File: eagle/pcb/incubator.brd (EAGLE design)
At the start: 99.1 x 63.5 mm, 56 parts, among them IC1 MCP1703-50, J2 RJ12RIGHTANGLE-I2C, J7 22--02, Q1 BSP75, Q5 BSP75, X2 8MHz, X4 MINI-USB

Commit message: routing in progress
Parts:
- added D2: 1N581D1206, lpatiny:LED-1206
- moved D4 15.1 mm to (75.6, 44.5), turned to 90 degrees
- moved D7 13.5 mm to (71.8, 44.5), turned to 90 degrees
- moved D1 13.1 mm to (81.9, 45.7), turned to 0 degrees
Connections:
- removed net N$3: CU7.1, D1.C, D4.C, D7.C, D8.C, IC1.1
- new net I2C+5V: D2.A, J2.+5V
- new net N$123: CU7.1, D1.C, D2.C, D4.C, D7.C, D8.C, IC1.1
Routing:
- net VUSB: track 104.6 -> 69.3 mm
- net D12*: track 0.00 -> 22.3 mm
- net N$3: track 0.55 -> 0.00 mm
- net N$123: track 0.00 -> 0.55 mm

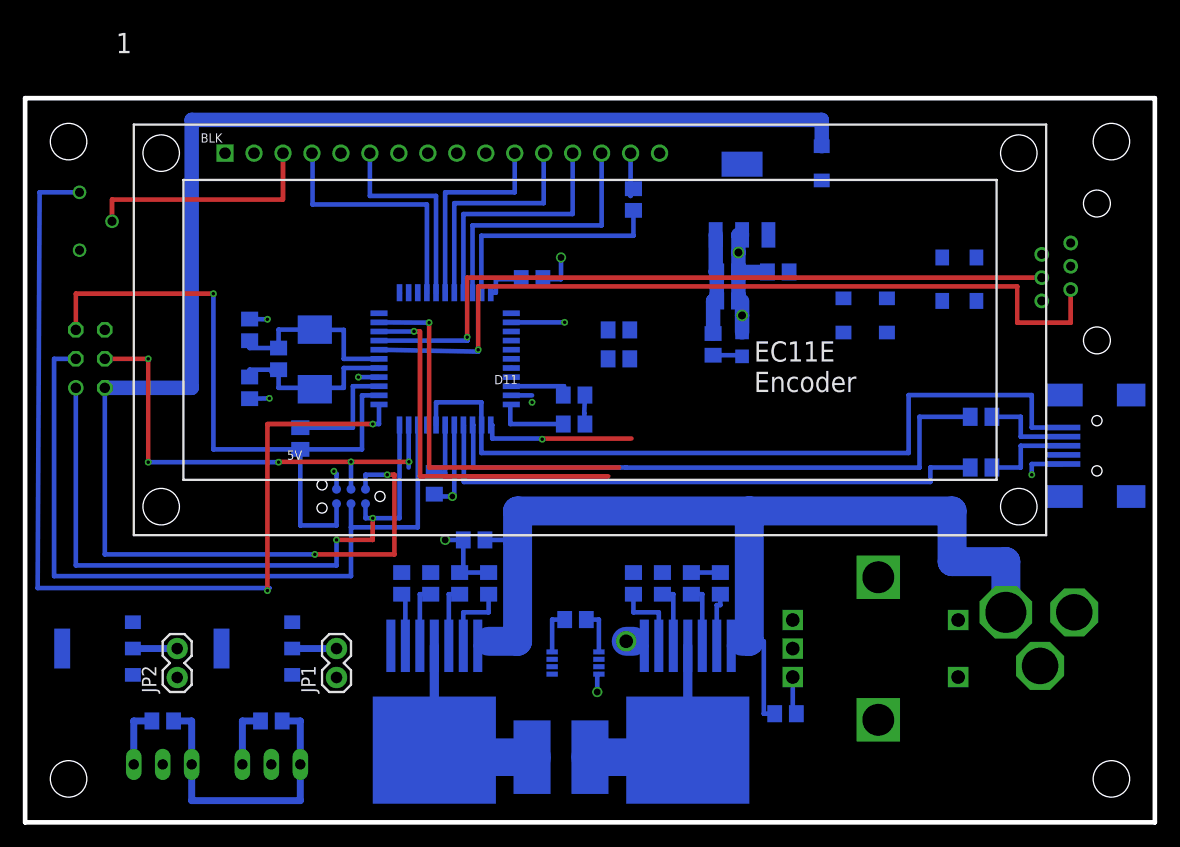
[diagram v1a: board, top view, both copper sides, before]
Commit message: first version of the incubator
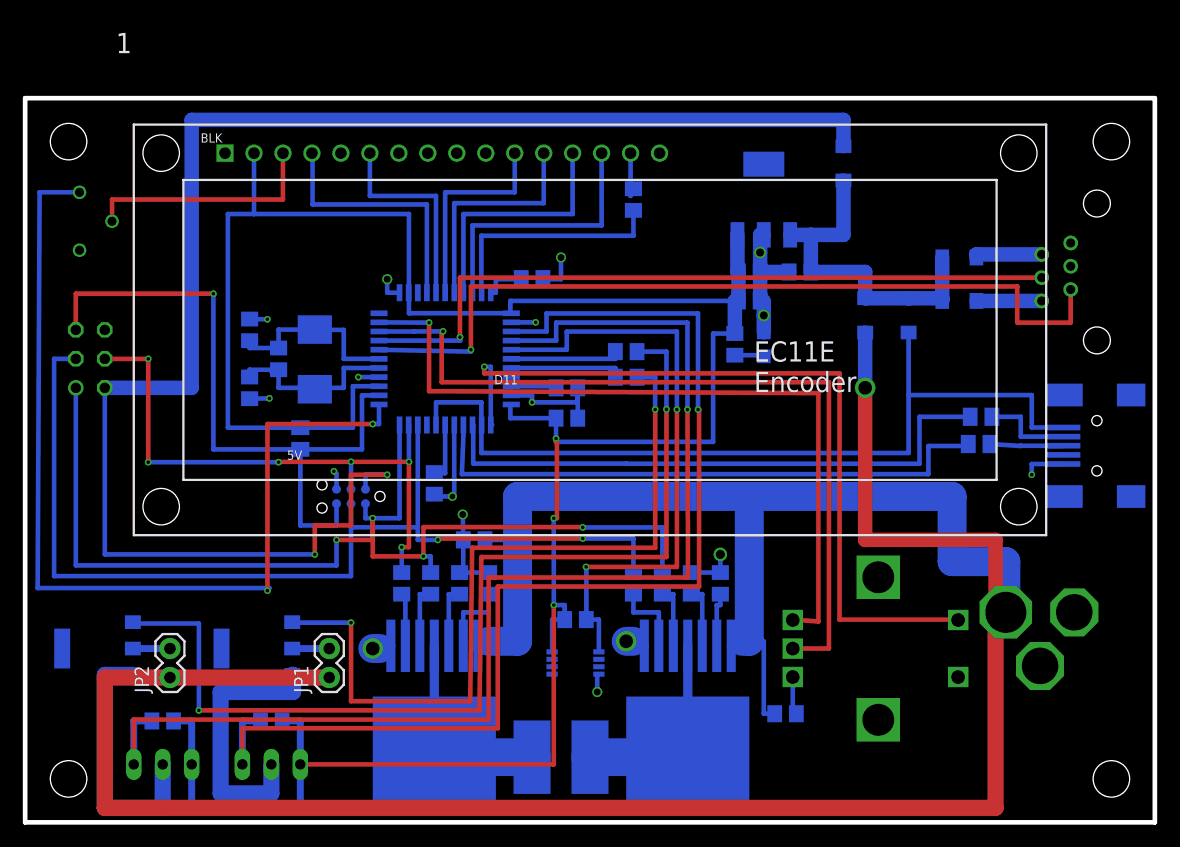
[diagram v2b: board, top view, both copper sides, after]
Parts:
- moved R1 4.20 mm to (52.7, 39.0), turned to 180 degrees
- moved RUSB2 2.06 mm to (83.6, 33.2)
- moved CU1 1.91 mm to (63.5, 45.7)
- moved CU8 1.91 mm to (63.5, 48.3)
- moved D4 1.91 mm to (77.5, 44.5)
- moved D7 1.91 mm to (73.7, 44.5)
- moved D8 1.91 mm to (71.8, 57.8)
- moved IC1 1.90 mm to (64.8, 54.6)
- moved LDPW5 1.90 mm to (64.8, 41.9)
- moved R13 1.90 mm to (62.2, 41.9)
- moved CU7 1.90 mm to (67.9, 48.3)
- moved C10 0.90 mm to (47.5, 38.1)
- moved R2 0.90 mm to (52.7, 41.3)
- moved C12 0.82 mm to (47.5, 35.4)
- moved JP2 0.64 mm to (12.7, 12.7)
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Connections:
- net A0: now also JP5.3, RT3.2; no longer R1.1
- net A1: now also JP4.3, RT1.2; no longer R2.1
- net A3: now also R2.1; no longer JP4.3, RT1.2
- net A4: now also R1.1; no longer JP5.3, RT3.2
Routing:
- net +12V: track 91.9 -> 258.9 mm, vias 0 -> 1
- net VCC: track 56.9 -> 223.5 mm, vias 0 -> 3
- net A1: track 0.00 -> 109.8 mm, vias 0 -> 1
- net A0: track 0.00 -> 103.0 mm, vias 0 -> 1
- net N$20: track 0.00 -> 88.4 mm, vias 0 -> 2
- net N$9: track 0.00 -> 68.6 mm, vias 0 -> 2
- net GND: track 60.3 -> 116.7 mm, vias 14 -> 17
- net D7*: track 13.7 -> 69.6 mm
- net A2: track 3.94 -> 53.3 mm, vias 0 -> 2
- net RX: track 32.8 -> 70.7 mm
- net MISO: track 58.2 -> 95.5 mm, vias 2 -> 4
- net TX: track 33.7 -> 66.9 mm
- net N$123: track 0.55 -> 30.9 mm
- net SCK: track 68.2 -> 91.3 mm, vias 0 -> 2
- net MOSI: track 41.9 -> 51.8 mm, vias 5 -> 6
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
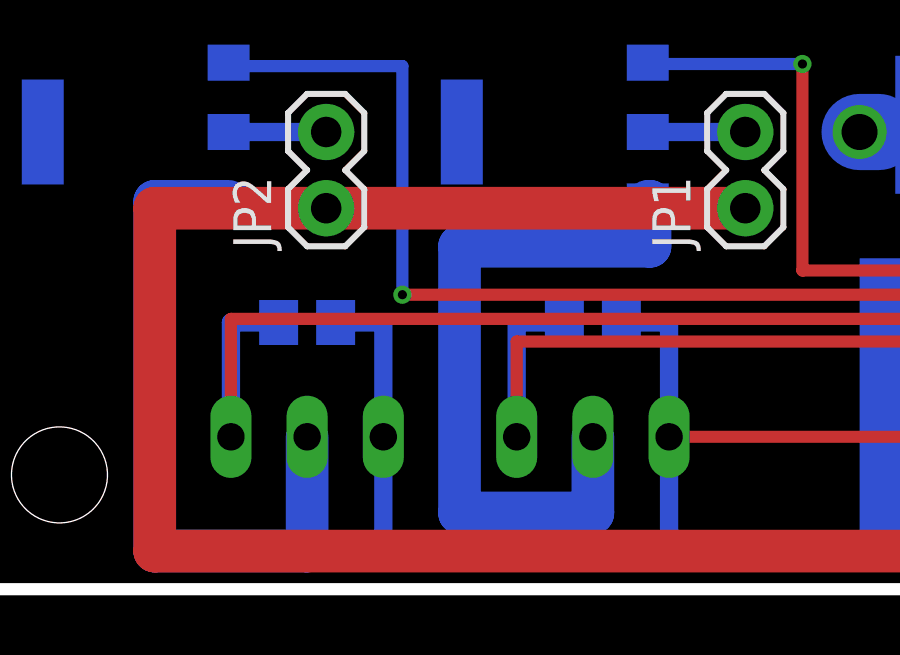
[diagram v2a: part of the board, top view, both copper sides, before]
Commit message: add test case and begin arduino program
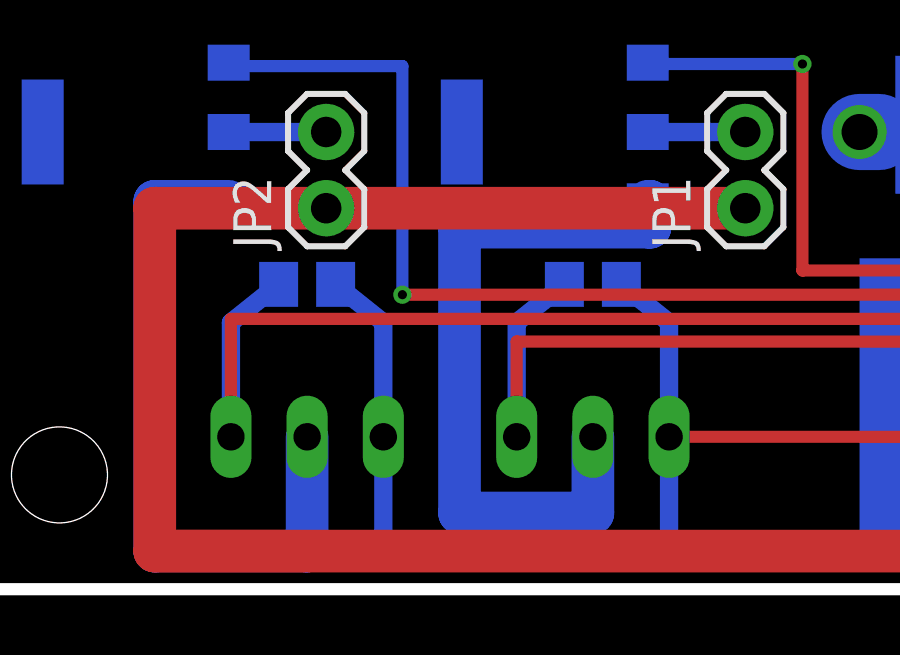
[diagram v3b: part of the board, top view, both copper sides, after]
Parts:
- moved RT1 1.27 mm to (12.1, 10.2)
- moved RT3 1.27 mm to (21.6, 10.2)
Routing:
- net VCC: track 223.5 -> 224.4 mm
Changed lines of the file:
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@@
 <?xml version="1.0" encoding="utf-8"?>
 <!DOCTYPE eagle SYSTEM "eagle.dtd">
-<eagle version="7.7.0">
+<eagle version="8.3.0">
 <drawing>
 <settings>
 <setting alwaysvectorfont="yes"/>
+<setting keepoldvectorfont="yes"/>
 <setting verticaltext="up"/>
 </settings>
@@
 </element>
 <element name="X4" library="con-cypressindustries" package="32005-201" value="MINI-USB" x="93.98" y="33.02" smashed="yes" rot="MR0">
+<attribute name="MF" value="" x="63.5" y="-33.02" size="1.778" layer="28" rot="MR0" display="off"/>
+<attribute name="MPN" value="" x="63.5" y="-33.02" size="1.778" layer="28" rot="MR0" display="off"/>
+<attribute name="NAME" x="93.70241875" y="26.520015625" size="1.27" layer="26" rot="MR90"/>
+<attribute name="OC_FARNELL" value="unknown" x="63.5" y="-33.02" size="1.778" layer="28" rot="MR0" display="off"/>
 <attribute name="OC_NEWARK" value="unknown" x="63.5" y="-33.02" size="1.778" layer="28" rot="MR0" display="off"/>
-<attribute name="MPN" value="" x="63.5" y="-33.02" size="1.778" layer="28" rot="MR0" display="off"/>
-<attribute name="MF" value="" x="63.5" y="-33.02" size="1.778" layer="28" rot="MR0" display="off"/>
-<attribute name="OC_FARNELL" value="unknown" x="63.5" y="-33.02" size="1.778" layer="28" rot="MR0" display="off"/>
-<attribute name="NAME" x="93.70241875" y="26.520015625" size="1.27" layer="26" rot="MR90"/>
 <attribute name="VALUE" x="98.425" y="26.035" size="1.27" layer="28" rot="MR0"/>
 </element>
@@
 <element name="D1" library="lpatiny" package="LED-1206" value="1N581D1206" x="81.915" y="45.72" rot="MR0"/>
 <element name="U$3" library="BTS7960" package="P-TO-263-7" value="BTS7960" x="30.48" y="17.78" rot="MR180">
+<attribute name="AVAILABILITY" value="Warning" x="30.48" y="17.78" size="1.778" layer="28" rot="MR180" display="off"/>
+<attribute name="DESCRIPTION" value="Half Bridge Motor Driver 7-Pin%286%2BTab%29 TO-263" x="30.48" y="17.78" size="1.778" layer="28" rot="MR180" display="off"/>
+<attribute name="MF" value="Infineon" x="30.48" y="17.78" size="1.778" layer="28" rot="MR180" display="off"/>
 <attribute name="MP" value="BTS7960B" x="30.48" y="17.78" size="1.778" layer="28" rot="MR180" display="off"/>
 <attribute name="PACKAGE" value="TO-263 Infineon" x="30.48" y="17.78" size="1.778" layer="28" rot="MR180" display="off"/>
-<attribute name="DESCRIPTION" value="Half Bridge Motor Driver 7-Pin%286%2BTab%29 TO-263" x="30.48" y="17.78" size="1.778" layer="28" rot="MR180" display="off"/>
 <attribute name="PRICE" value="4.95 USD" x="30.48" y="17.78" size="1.778" layer="28" rot="MR180" display="off"/>
-<attribute name="MF" value="Infineon" x="30.48" y="17.78" size="1.778" layer="28" rot="MR180" display="off"/>
-<attribute name="AVAILABILITY" value="Warning" x="30.48" y="17.78" size="1.778" layer="28" rot="MR180" display="off"/>
 </element>
 <element name="U$4" library="BTS7960" package="P-TO-263-7" value="BTS7960" x="52.705" y="17.78" rot="MR180">
+<attribute name="AVAILABILITY" value="Warning" x="52.705" y="17.78" size="1.778" layer="28" rot="MR180" display="off"/>
+<attribute name="DESCRIPTION" value="Half Bridge Motor Driver 7-Pin%286%2BTab%29 TO-263" x="52.705" y="17.78" size="1.778" layer="28" rot="MR180" display="off"/>
+<attribute name="MF" value="Infineon" x="52.705" y="17.78" size="1.778" layer="28" rot="MR180" display="off"/>
 <attribute name="MP" value="BTS7960B" x="52.705" y="17.78" size="1.778" layer="28" rot="MR180" display="off"/>
 <attribute name="PACKAGE" value="TO-263 Infineon" x="52.705" y="17.78" size="1.778" layer="28" rot="MR180" display="off"/>
-<attribute name="DESCRIPTION" value="Half Bridge Motor Driver 7-Pin%286%2BTab%29 TO-263" x="52.705" y="17.78" size="1.778" layer="28" rot="MR180" display="off"/>
 <attribute name="PRICE" value="4.95 USD" x="52.705" y="17.78" size="1.778" layer="28" rot="MR180" display="off"/>
-<attribute name="MF" value="Infineon" x="52.705" y="17.78" size="1.778" layer="28" rot="MR180" display="off"/>
-<attribute name="AVAILABILITY" value="Warning" x="52.705" y="17.78" size="1.778" layer="28" rot="MR180" display="off"/>
 </element>
 <element name="RXT1" library="rcl" package="R0805" value="10k" x="38.1" y="20.955" smashed="yes" rot="MR270">
@@
 <element name="POWER" library="lpatiny" package="DC_BARREL" value="JACK_DC_BARREL" x="99.695" y="18.415" rot="MR270"/>
 <element name="Q5" library="infineon" package="PG-SOT-223" value="BSP75" x="20.32" y="15.24" rot="MR270">
+<attribute name="MF" value="" x="20.32" y="15.24" size="1.778" layer="28" rot="MR270" display="off"/>
 <attribute name="MPN" value="" x="20.32" y="15.24" size="1.778" layer="28" rot="MR270" display="off"/>
 <attribute name="OC_FARNELL" value="unknown" x="20.32" y="15.24" size="1.778" layer="28" rot="MR270" display="off"/>
-<attribute name="MF" value="" x="20.32" y="15.24" size="1.778" layer="28" rot="MR270" display="off"/>
 <attribute name="OC_NEWARK" value="unknown" x="20.32" y="15.24" size="1.778" layer="28" rot="MR270" display="off"/>
 </element>
 <element name="R1" library="rcl" package="R0805" value="1K" x="52.705" y="39.0271" rot="MR180"/>
 <element name="Q1" library="infineon" package="PG-SOT-223" value="BSP75" x="6.35" y="15.24" rot="MR270">
+<attribute name="MF" value="" x="6.35" y="15.24" size="1.778" layer="28" rot="MR270" display="off"/>
 <attribute name="MPN" value="" x="6.35" y="15.24" size="1.778" layer="28" rot="MR270" display="off"/>
 <attribute name="OC_FARNELL" value="unknown" x="6.35" y="15.24" size="1.778" layer="28" rot="MR270" display="off"/>
-<attribute name="MF" value="" x="6.35" y="15.24" size="1.778" layer="28" rot="MR270" display="off"/>
 <attribute name="OC_NEWARK" value="unknown" x="6.35" y="15.24" size="1.778" layer="28" rot="MR270" display="off"/>
 </element>
@@
 <element name="JP4" library="jumper" package="JP2" value="" x="12.065" y="5.08" rot="MR0"/>
 <element name="JP5" library="jumper" package="JP2" value="" x="21.59" y="5.08" rot="MR0"/>
-<element name="RT1" library="resistor" package="R0805" value="4.7k" x="12.065" y="8.89" rot="MR0"/>
-<element name="RT3" library="resistor" package="R0805" value="4.7k" x="21.59" y="8.89" rot="MR0"/>
+<element name="RT1" library="resistor" package="R0805" value="4.7k" x="12.065" y="10.16" rot="MR0"/>
+<element name="RT3" library="resistor" package="R0805" value="4.7k" x="21.59" y="10.16" rot="MR0"/>
 <element name="RXT8" library="rcl" package="R0805" value="10k" x="40.64" y="20.955" smashed="yes" rot="MR90">
 <attribute name="NAME" x="41.91" y="20.32" size="1.27" layer="26" rot="MR90"/>
@@
 <wire x1="12.065" y1="1.27" x2="12.065" y2="5.08" width="1.4224" layer="16"/>
 <wire x1="23.419" y1="12.929" x2="23.495" y2="12.929" width="1.4224" layer="16"/>
-<wire x1="23.495" y1="12.929" x2="23.495" y2="11.43" width="1.4224" layer="16"/>
-<wire x1="23.495" y1="11.43" x2="17.145" y2="11.43" width="1.4224" layer="16"/>
-<wire x1="17.145" y1="11.43" x2="17.145" y2="2.54" width="1.4224" layer="16"/>
+<wire x1="23.495" y1="12.929" x2="23.495" y2="12.065" width="1.4224" layer="16"/>
+<wire x1="23.495" y1="12.065" x2="17.145" y2="12.065" width="1.4224" layer="16"/>
+<wire x1="17.145" y1="12.065" x2="17.145" y2="2.54" width="1.4224" layer="16"/>
 <wire x1="17.145" y1="2.54" x2="21.59" y2="2.54" width="1.4224" layer="16"/>
 <wire x1="21.59" y1="2.54" x2="21.59" y2="5.08" width="1.4224" layer="16"/>
@@
 <contactref element="JP4" pad="3"/>
 <contactref element="RT1" pad="2"/>
-<wire x1="11.115" y1="8.89" x2="9.525" y2="8.89" width="0.6096" layer="16"/>
+<wire x1="11.115" y1="10.16" x2="9.525" y2="8.89" width="0.6096" layer="16"/>
 <wire x1="9.525" y1="8.89" x2="9.525" y2="5.08" width="0.6096" layer="16"/>
 <wire x1="46.56455" y1="42.24" x2="46.56455" y2="43.815" width="0.4064" layer="16"/>
@@
 <contactref element="JP5" pad="3"/>
 <contactref element="RT3" pad="2"/>
-<wire x1="20.64" y1="8.89" x2="19.05" y2="8.89" width="0.6096" layer="16"/>
+<wire x1="20.64" y1="10.16" x2="19.05" y2="8.89" width="0.6096" layer="16"/>
 <wire x1="19.05" y1="8.89" x2="19.05" y2="5.08" width="0.6096" layer="16"/>
 <wire x1="45.72" y1="43.04" x2="45.72" y2="44.62145" width="0.4064" layer="16"/>
@@
 <contactref element="RT1" pad="1"/>
 <contactref element="U$11" pad="2"/>
-<wire x1="13.015" y1="8.89" x2="14.605" y2="8.89" width="0.6096" layer="16"/>
+<wire x1="13.015" y1="10.16" x2="14.605" y2="8.89" width="0.6096" layer="16"/>
 <wire x1="14.605" y1="8.89" x2="14.605" y2="5.08" width="0.6096" layer="16"/>
-<wire x1="22.54" y1="8.89" x2="24.13" y2="8.89" width="0.6096" layer="16"/>
+<wire x1="22.54" y1="10.16" x2="24.13" y2="8.89" width="0.6096" layer="16"/>
 <wire x1="24.13" y1="8.89" x2="24.13" y2="5.08" width="0.6096" layer="16"/>
 <wire x1="24.13" y1="5.08" x2="24.13" y2="0.9271" width="0.6096" layer="16"/>

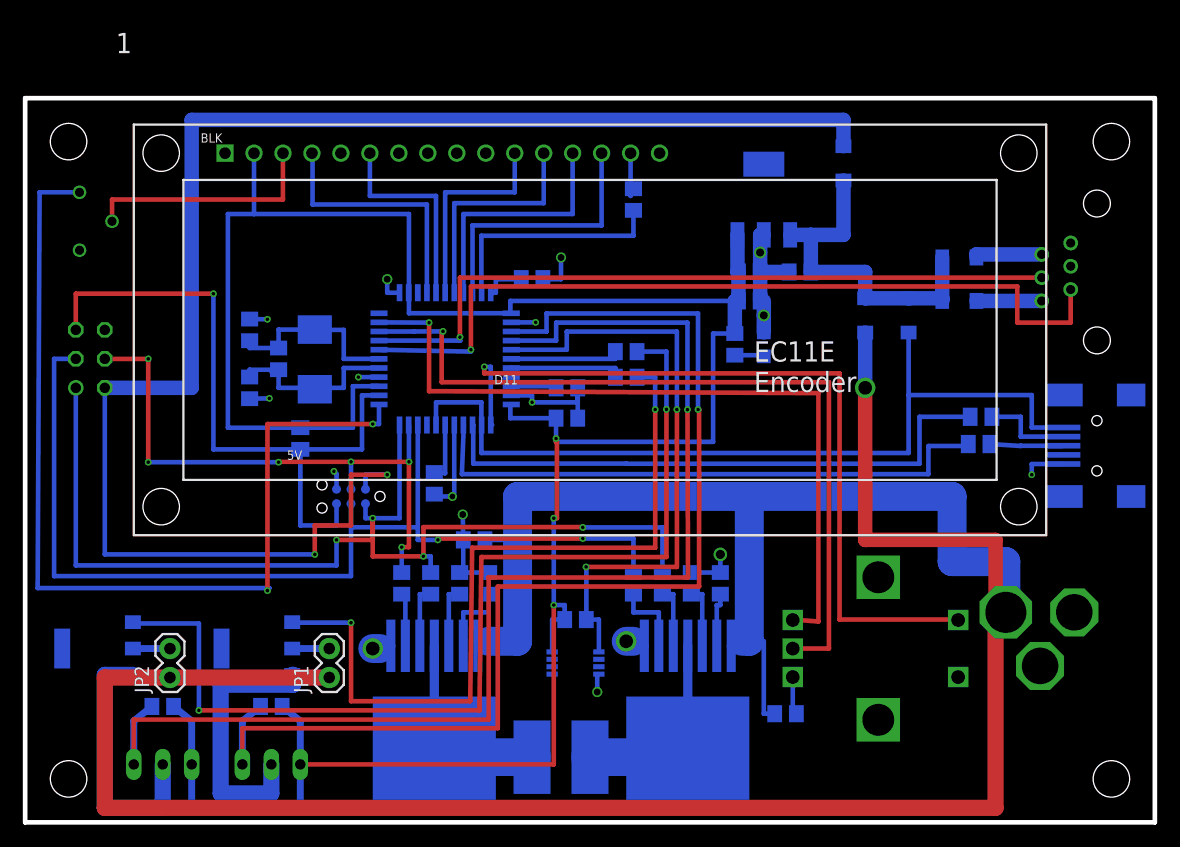
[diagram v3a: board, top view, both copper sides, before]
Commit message: 45 degree traces
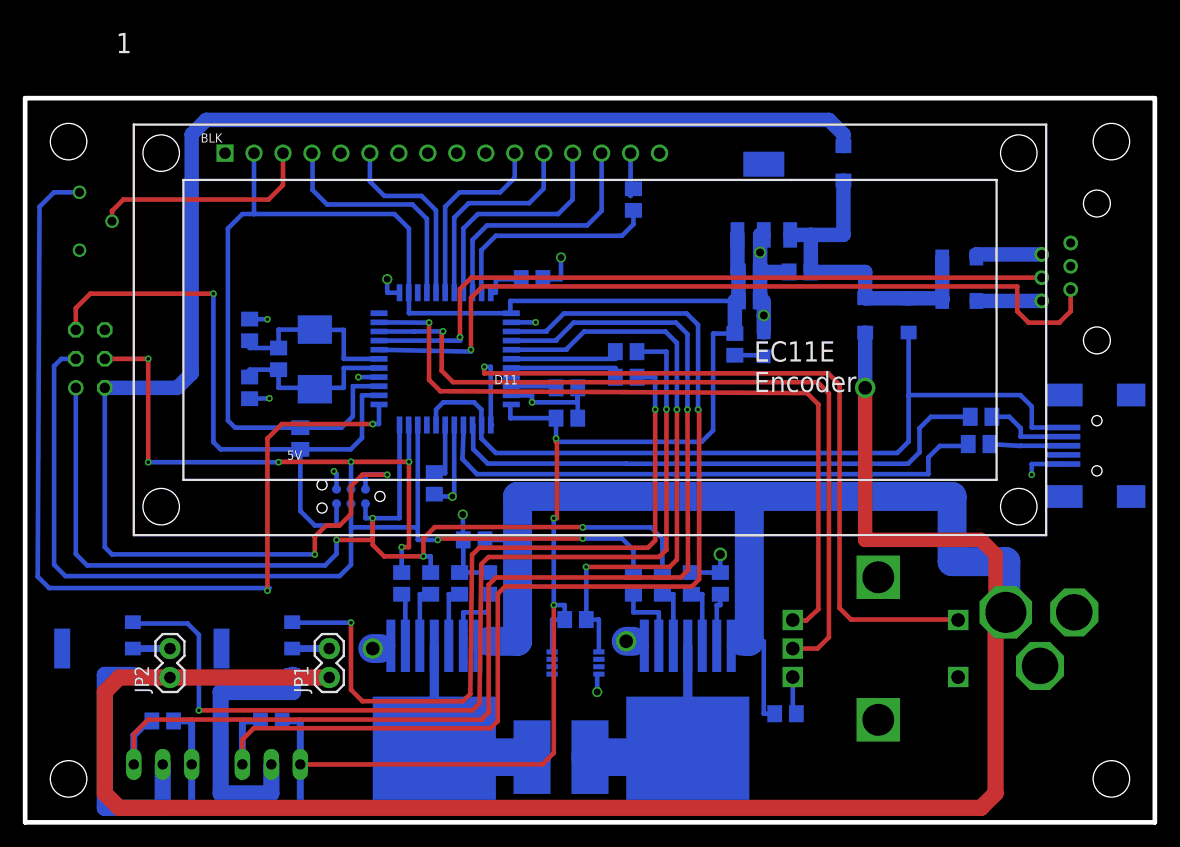
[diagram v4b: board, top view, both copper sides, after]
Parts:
- moved RT1 1.27 mm to (12.1, 8.89)
- moved RT3 1.27 mm to (21.6, 8.89)
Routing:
- net A1: track 110.2 -> 105.7 mm
- net VCC: track 224.4 -> 219.9 mm
- net ISP+5V: track 140.1 -> 135.7 mm
- net A0: track 103.5 -> 99.9 mm
- net +12V: track 258.9 -> 255.9 mm
- net MISO: track 95.5 -> 92.6 mm
- net VUSB: track 74.8 -> 72.2 mm
- net RESET: track 59.9 -> 57.4 mm
- net SCK: track 91.3 -> 89.2 mm
- net D11*: track 84.9 -> 82.8 mm
- net USB_N: track 51.1 -> 49.2 mm
- net A2: track 53.3 -> 51.4 mm
- net TX: track 66.9 -> 65.0 mm
- net SCL: track 72.4 -> 70.7 mm
- net RX: track 70.7 -> 68.9 mm
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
